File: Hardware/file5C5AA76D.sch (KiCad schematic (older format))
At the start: 16 parts, among them J14 Conn_01x04_Female, U5 MAX7375AXR105, U6 74HC595, U7 74HC595, U8 SID

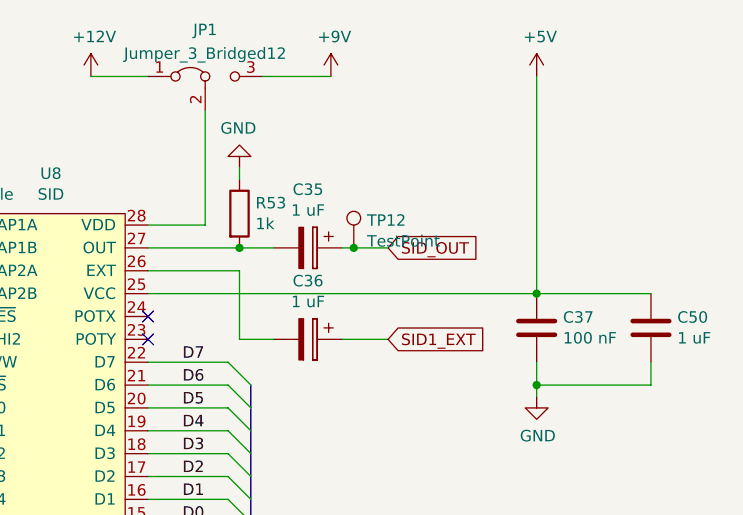
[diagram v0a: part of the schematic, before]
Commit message: Finished design of 4 layer, added stero option and logo
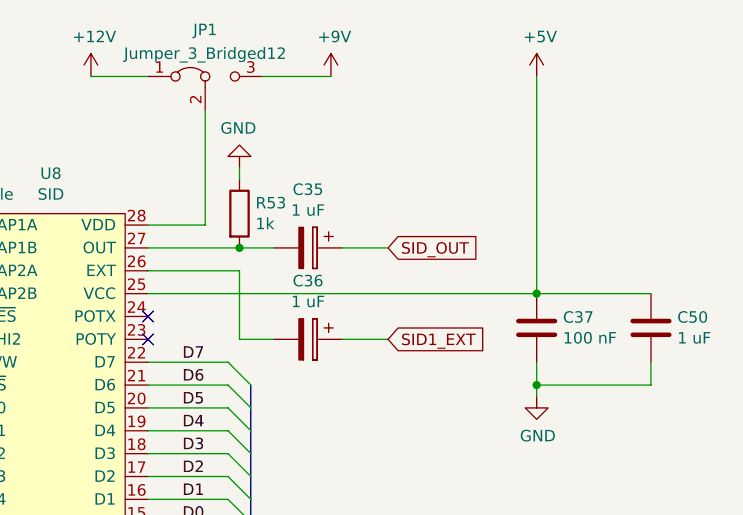
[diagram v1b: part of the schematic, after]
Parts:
- removed TP12: TestPoint, TestPoint:TestPoint_Pad_D1.0mm, symbol Connector:TestPoint
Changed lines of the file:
@@
 	4000 3550 4000 3600
 Wire Wire Line
-	8350 2250 8400 2250
-$Comp
-L Connector:TestPoint TP12
-U 1 1 5CBB3BCE
-P 8400 2250
-F 0 "TP12" H 8458 2370 50  0000 L CNN
-F 1 "TestPoint" H 8458 2279 50  0000 L CNN
-F 2 "TestPoint:TestPoint_Pad_D1.0mm" H 8600 2250 50  0001 C CNN
-F 3 "~" H 8600 2250 50  0001 C CNN
-	1    8400 2250
-	1    0    0    -1
-$EndComp
-Connection ~ 8400 2250
-Wire Wire Line
-	8400 2250 8550 2250
+	8350 2250 8550 2250
 Wire Bus Line
 	6200 3050 6200 4050
